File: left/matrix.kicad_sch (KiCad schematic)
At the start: 64 parts

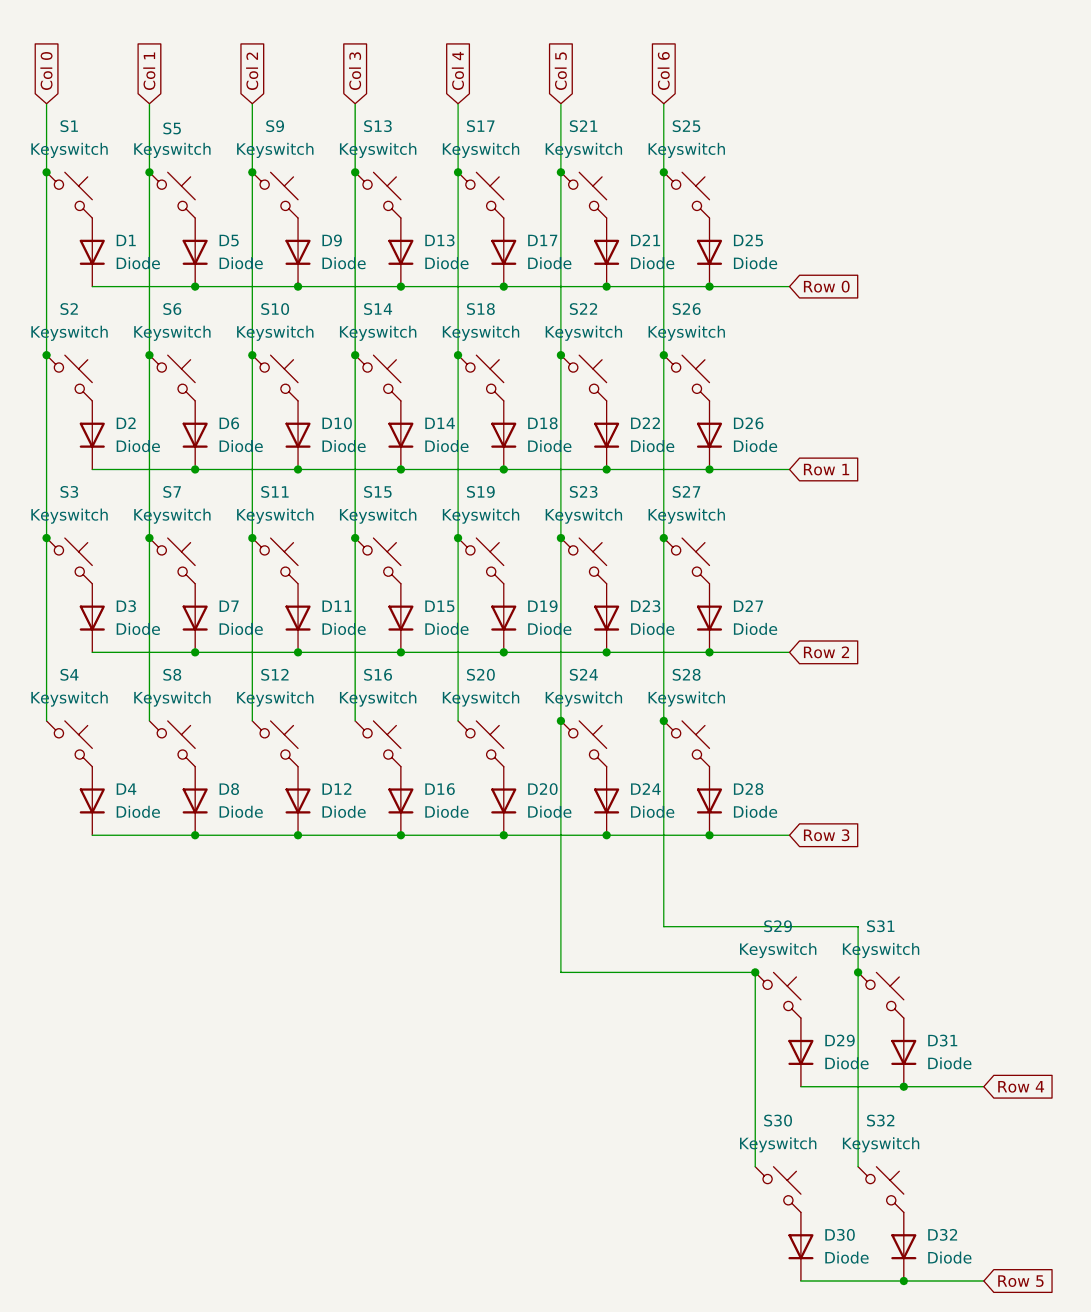
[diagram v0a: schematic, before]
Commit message: Fix issues from update to KiCad 9
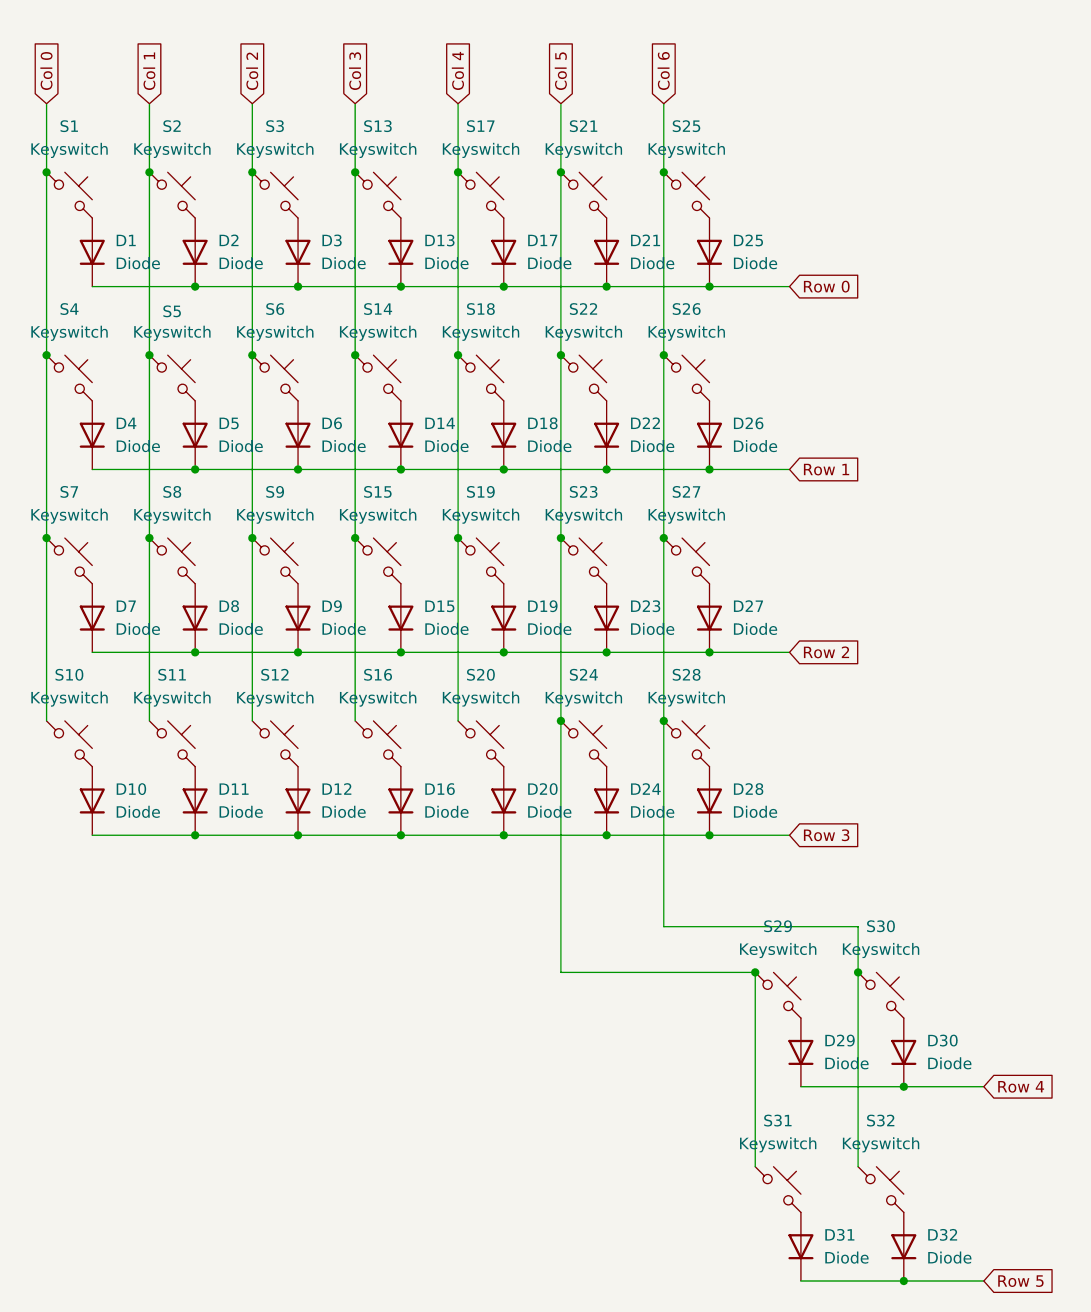
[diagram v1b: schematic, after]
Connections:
- net Col 0: now also S10.1, S7.1; no longer S2.1, S3.1
- net Col 1: now also S11.1, S2.1; no longer S6.1, S7.1
- net Col 2: now also S3.1, S6.1; no longer S10.1, S11.1
- net Col 5: now also S31.1; no longer S30.1
- net Col 6: now also S30.1; no longer S31.1
- net Row 0: now also D2.1 (K), D3.1 (K); no longer D5.1 (K), D9.1 (K)
- net Row 1: now also D4.1 (K), D5.1 (K); no longer D10.1 (K), D2.1 (K)
- net Row 2: now also D8.1 (K), D9.1 (K); no longer D11.1 (K), D3.1 (K)
- net Row 3: now also D10.1 (K), D11.1 (K); no longer D4.1 (K), D8.1 (K)
- net Row 4: now also D30.1 (K); no longer D31.1 (K)
- net Row 5: now also D31.1 (K); no longer D30.1 (K)
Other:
- moved on the sheet: D10, D11, D2, D3, D30, D31, D4, D5, D6, D7, D8, D9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
